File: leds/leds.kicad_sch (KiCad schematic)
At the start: 51 parts, among them J101 Conn_02x05_Odd_Even, J102 Conn_02x05_Odd_Even

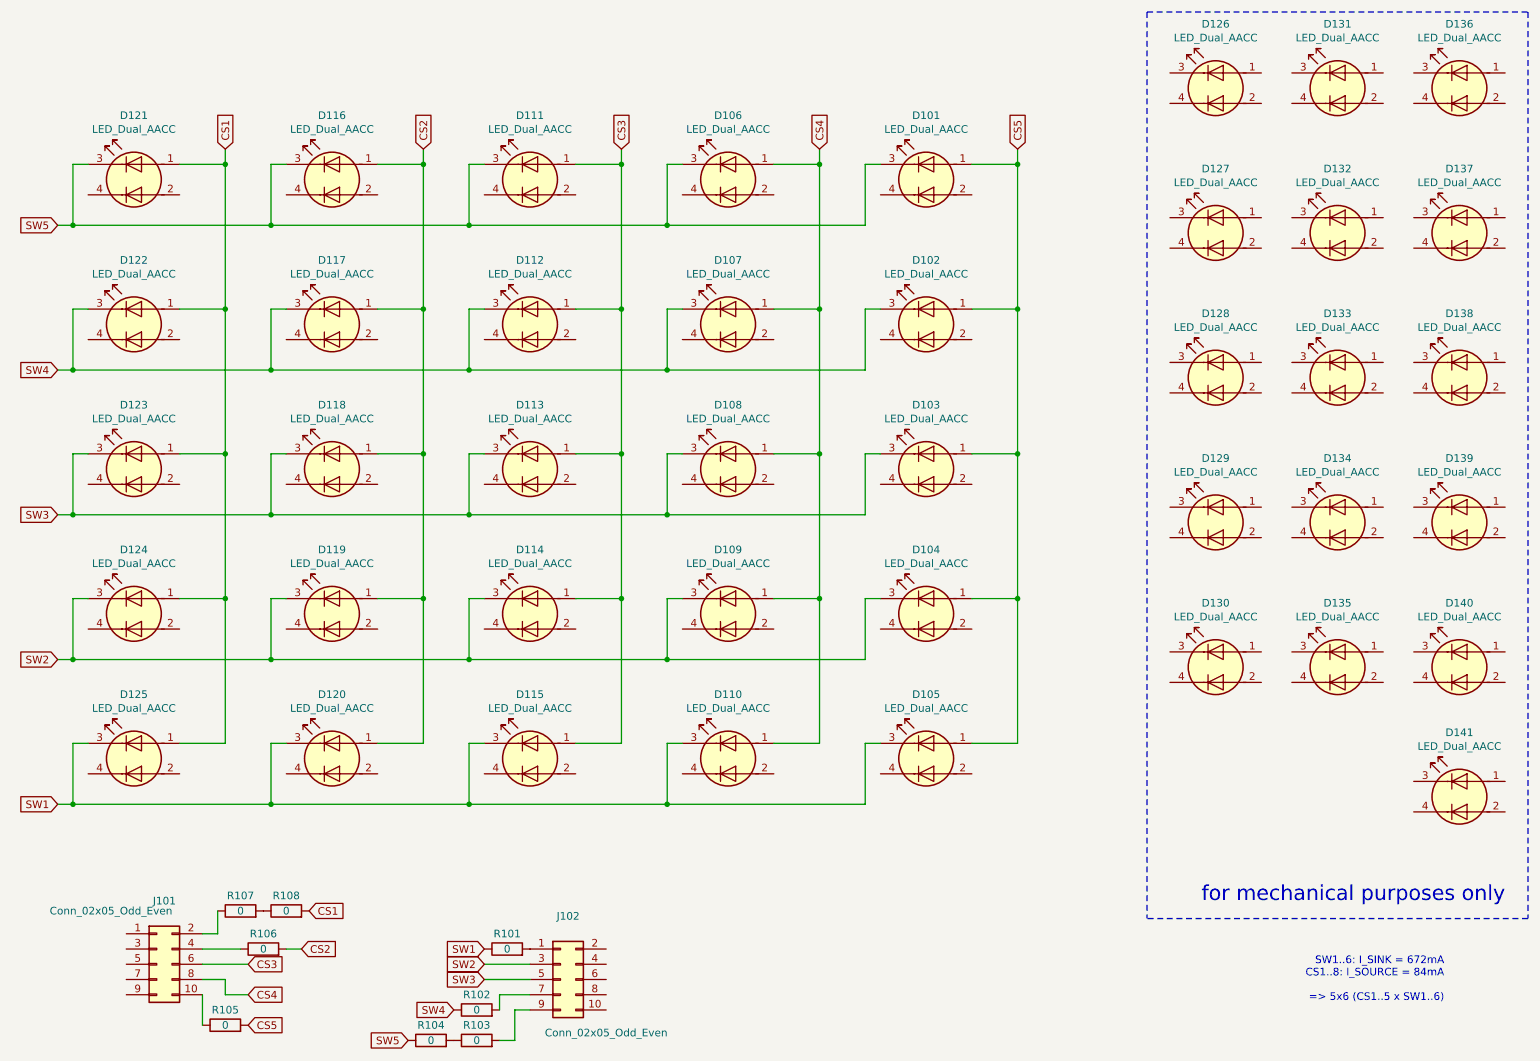
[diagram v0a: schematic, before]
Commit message: remove unused LEDs, add paste in gerber output
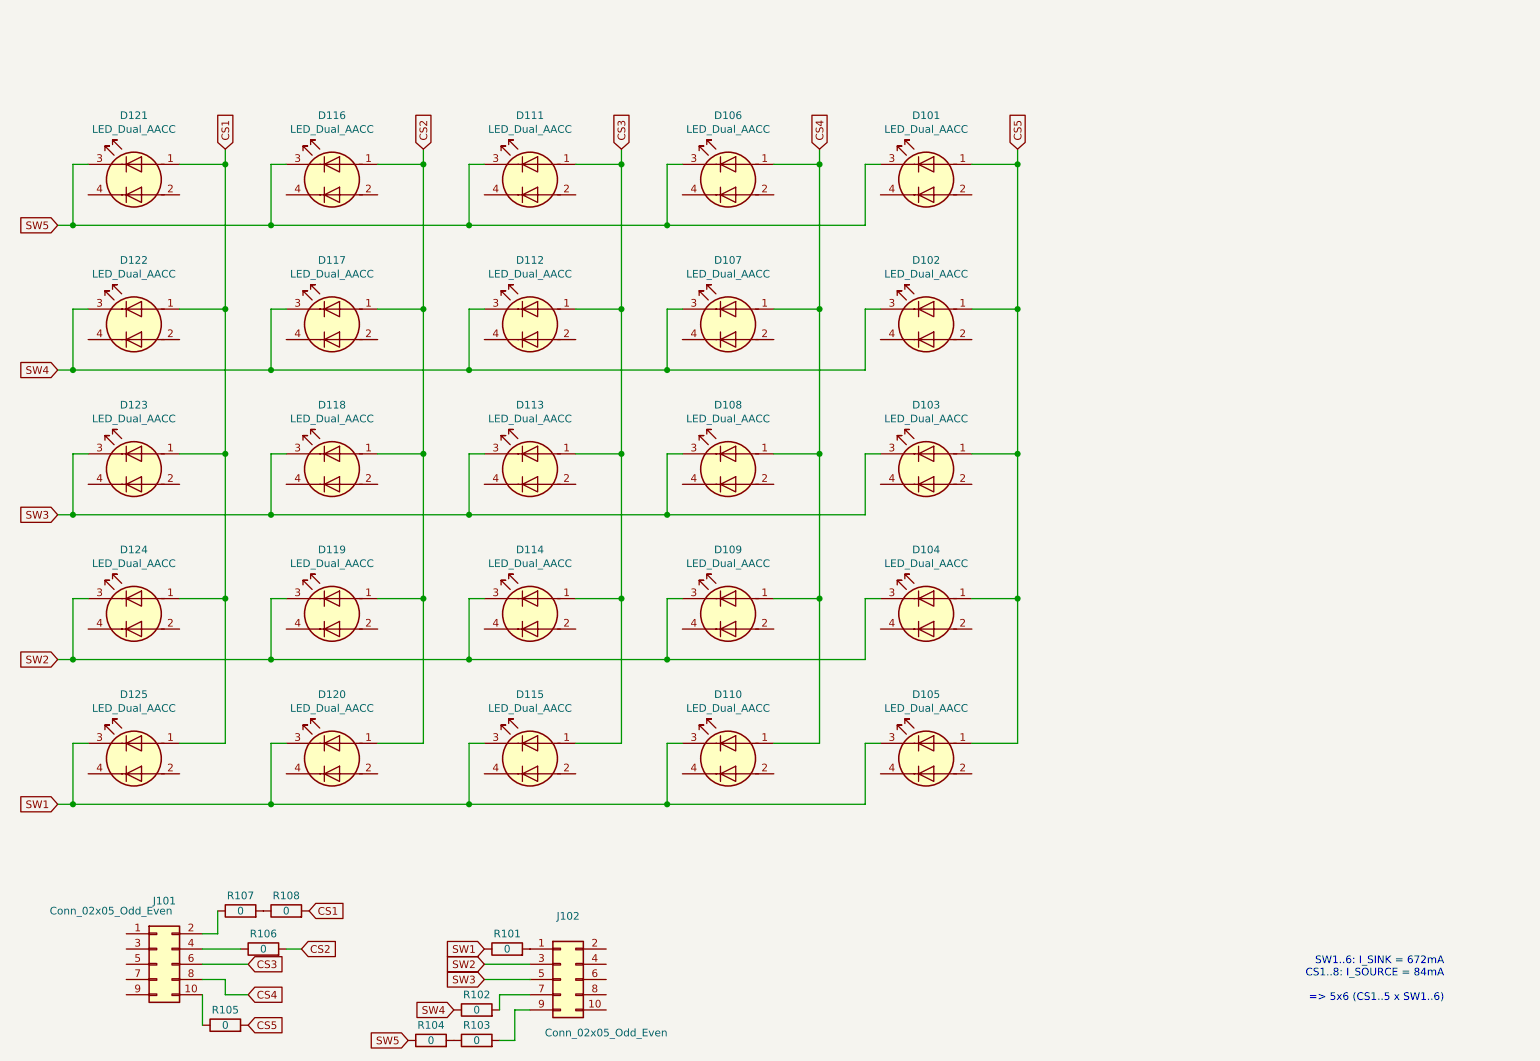
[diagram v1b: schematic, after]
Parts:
- removed D126, D127, D128, D129, D130, D131, D132, D133, D134, D135, D136, D137, D138, D139, D140, D141: LED_Dual_AACC, leds:Wuerth_150141RV73100, symbol Device:LED_Dual_AACC
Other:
- note removed: "for mechanical purposes only"

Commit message: add doc-fields in schematics, add PDFs of schematics
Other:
- company: (none) -> hunz <hunz@mailbox.org>
- title: (none) -> Exposure Notifications LED matrix
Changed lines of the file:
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@@
   (page 1 1)
   (paper "A4")
+  (title_block
+    (title "Exposure Notifications LED matrix")
+    (rev "1b")
+    (company "hunz <hunz@mailbox.org>")
+  )
   (junction (at 40.64 48.26) (diameter 1.016) (color 0 0 0 0))
   (junction (at 40.64 72.39) (diameter 1.016) (color 0 0 0 0))
@@
   )
   (text "SW1..6: I_SINK = 672mA\nCS1..8: I_SOURCE = 84mA\n\n=> 5x6 (CS1..5 x SW1..6)"
-    (at 269.24 177.8 0)
+    (at 251.46 156.21 0)
     (effects (font (size 1.27 1.27)) (justify right bottom))
   )
